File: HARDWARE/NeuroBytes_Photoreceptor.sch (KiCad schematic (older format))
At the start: 21 parts, among them P1 CONN_01X04, P2 CONN_01X04, P3 CONN_01X07, SW1 SW_PUSH, SW2 SW_PUSH, U1 APDS9007, U2 STM32L011Gx, U3 LD3985M33R

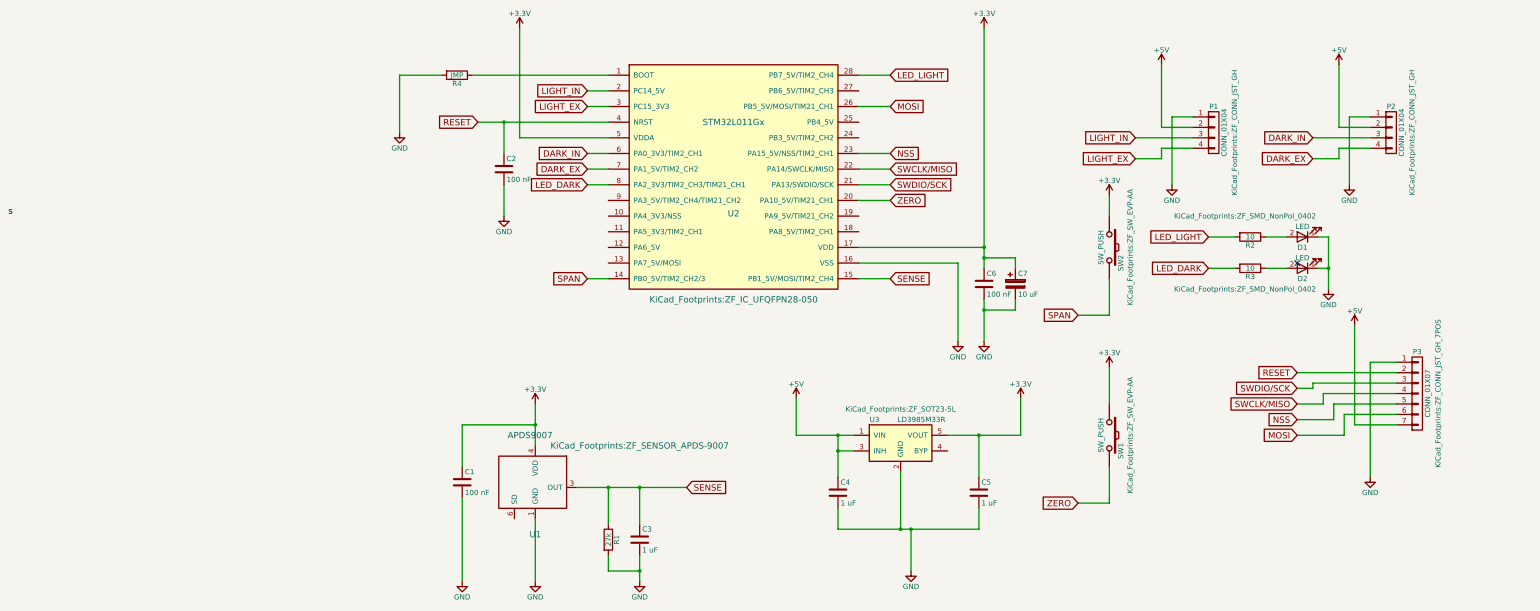
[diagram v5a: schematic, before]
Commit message: Another switch footprint update
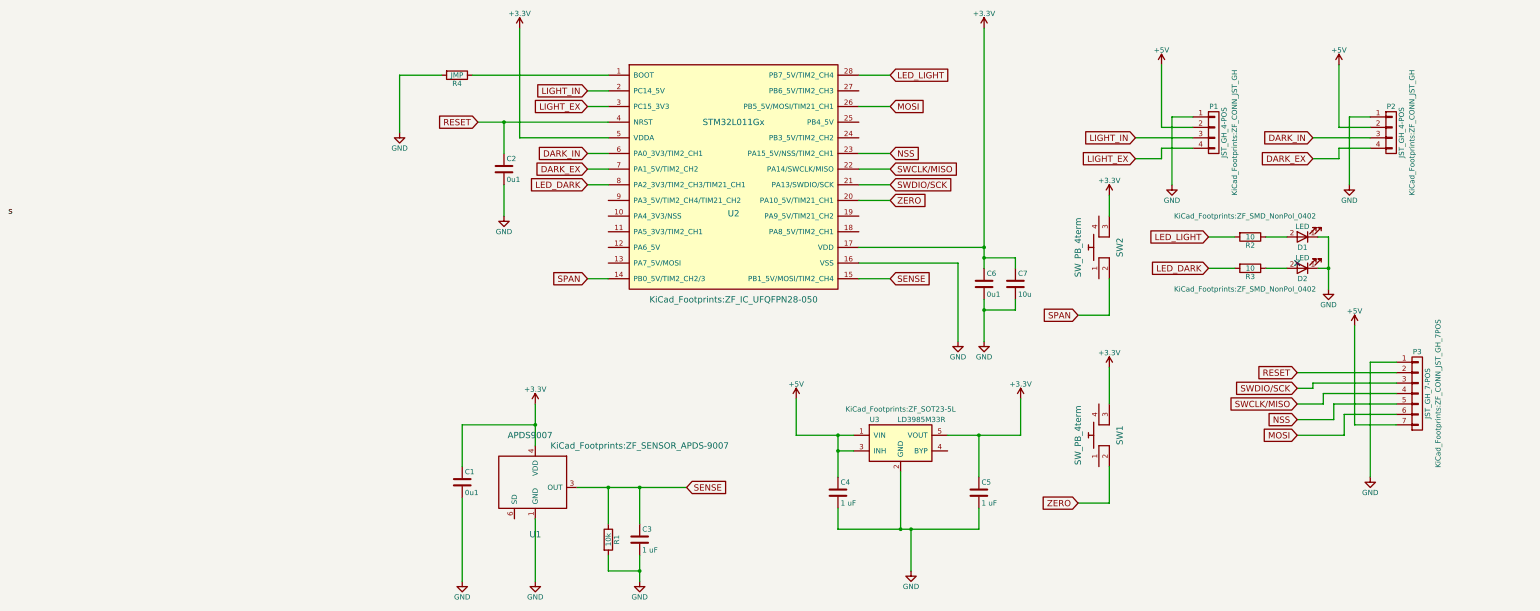
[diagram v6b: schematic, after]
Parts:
- removed C7: 10 uF, KiCad_Footprints:ZF_SMD_pol_1206, symbol CP
- removed SW1, SW2: SW_PUSH, KiCad_Footprints:ZF_SW_EVP-AA, symbol SW_PUSH
- added C7: 10u, KiCad_Footprints:ZF_SMD_nonpol_1206, symbol C
- added SW1, SW2: SW_PB_4term, KiCad_Footprints:ZF_SW_PTS810, symbol SW_PB_4term
- C1, C2, C6: value 100 nF -> 0u1; Mfr Part # (none) -> MF-CAP-0402-0.1uF; Package (none) -> C0402
- C3, C4, C5: Mfr Part # (none) -> MF-CAP-0603-1uF; Package (none) -> C0603
- D1, D2: Mfr Part # (none) -> SCMP13WBC8W1; Package (none) -> 2SMD
- P1, P2: value CONN_01X04 -> JST_GH_4-POS; Mfr Part # (none) -> SM04B-GHS-GD-TB(LF)(SN); Package (none) -> JST_GH_4-POS
- P3: value CONN_01X07 -> JST_GH_7-POS; Mfr Part # (none) -> SM07B-GHS-TB(LF)(SN); Package (none) -> JST_GH_7-POS
- R1: value 27k -> 10k; Mfr Part # (none) -> MF-RES-0402-10K; Package (none) -> R0402
- R2, R3: Mfr Part # (none) -> MF-RES-0402-10; Package (none) -> R0402
- R4: Mfr Part # (none) -> MF-RES-0402-0; Package (none) -> R0402
- U1: Mfr Part # (none) -> APDS-9007-020; Package (none) -> 6SMD
- U2: Mfr Part # (none) -> STM32L011G4U6; Package (none) -> UFQFPN28
- U3: Mfr Part # (none) -> MF-REG-SOT235-3.3V-300mA; Package (none) -> SOT23-5L
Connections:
- net +3V3: now also C7.1, SW1.3, SW2.3
- net GND: now also C7.2
- net SPAN: now also SW2.2
- net ZERO: now also SW1.2

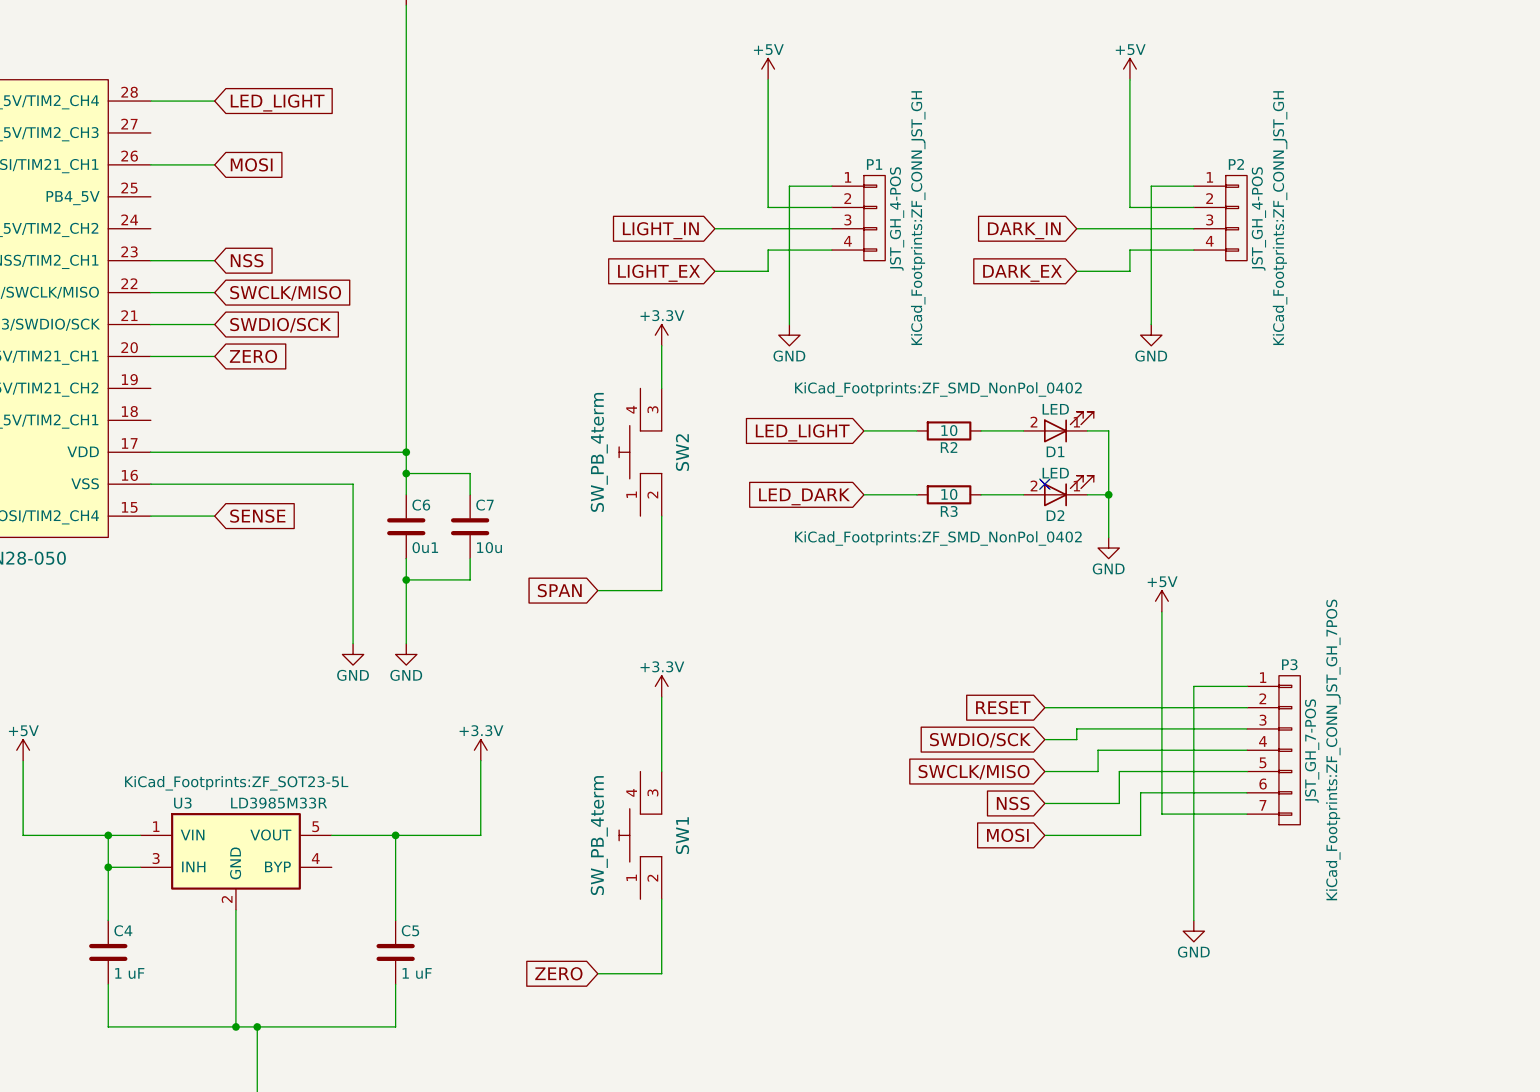
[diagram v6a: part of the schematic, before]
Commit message: Changed to 5-pin JST GH connector for programming and power. Added POWER label. Minor routing changes.
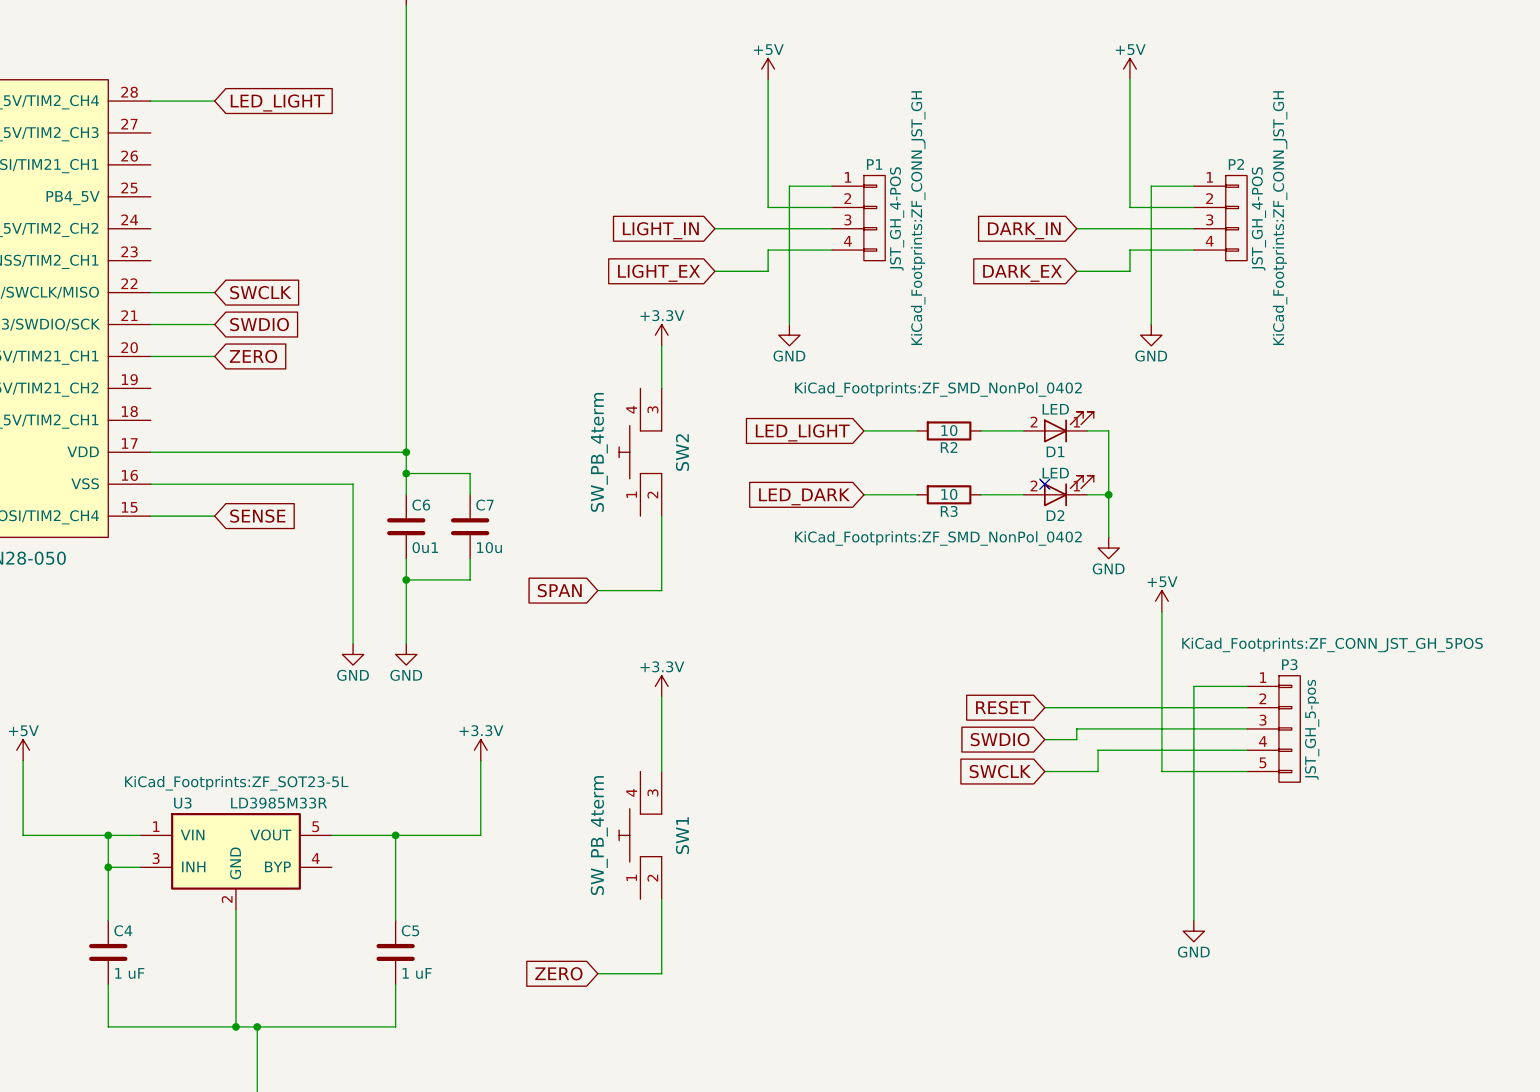
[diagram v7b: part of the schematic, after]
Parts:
- removed P3: JST_GH_7-POS, KiCad_Footprints:ZF_CONN_JST_GH_7POS, symbol CONN_01X07
- added P3: JST_GH_5-pos, KiCad_Footprints:ZF_CONN_JST_GH_5POS, symbol CONN_01X05
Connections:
- net +5V: now also P3.5 (P5)
- net GND: now also P3.1 (P1)
- net RESET: now also P3.2 (P2)
- net MOSI: no longer names the net of U2.26 (PB5_5V/MOSI/TIM21_CH1)
- net NSS: no longer names the net of U2.23 (PA15_5V/NSS/TIM2_CH1)
- net SWCLK/MISO renamed SWCLK
- net SWCLK: now also P3.4 (P4)
- net SWDIO/SCK renamed SWDIO
- net SWDIO: now also P3.3 (P3)
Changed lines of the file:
@@
 $EndComp
 $Comp
-L +5V #PWR01
+L +5V #PWR8
 U 1 1 58B9AB7F
 P 4700 4850
-F 0 "#PWR01" H 4700 4700 50  0001 C CNN
+F 0 "#PWR8" H 4700 4700 50  0001 C CNN
 F 1 "+5V" H 4700 4990 50  0000 C CNN
 F 2 "" H 4700 4850 50  0000 C CNN
@@
 $EndComp
 $Comp
-L +3.3V #PWR02
+L +3.3V #PWR13
 U 1 1 58B9B0DC
 P 6850 4850
-F 0 "#PWR02" H 6850 4700 50  0001 C CNN
+F 0 "#PWR13" H 6850 4700 50  0001 C CNN
 F 1 "+3.3V" H 6850 4990 50  0000 C CNN
 F 2 "" H 6850 4850 50  0000 C CNN
@@
 $EndComp
 $Comp
-L GND #PWR03
+L GND #PWR9
 U 1 1 58B9B110
 P 5800 6500
-F 0 "#PWR03" H 5800 6250 50  0001 C CNN
+F 0 "#PWR9" H 5800 6250 50  0001 C CNN
 F 1 "GND" H 5800 6350 50  0000 C CNN
 F 2 "" H 5800 6500 50  0000 C CNN
@@
 $EndComp
 $Comp
-L +3.3V #PWR04
+L +3.3V #PWR4
 U 1 1 58B9B1C8
 P 2050 1300
-F 0 "#PWR04" H 2050 1150 50  0001 C CNN
+F 0 "#PWR4" H 2050 1150 50  0001 C CNN
 F 1 "+3.3V" H 2050 1440 50  0000 C CNN
 F 2 "" H 2050 1300 50  0000 C CNN
@@
 $EndComp
 $Comp
-L +3.3V #PWR05
+L +3.3V #PWR11
 U 1 1 58B9B218
 P 6500 1300
-F 0 "#PWR05" H 6500 1150 50  0001 C CNN
+F 0 "#PWR11" H 6500 1150 50  0001 C CNN
 F 1 "+3.3V" H 6500 1440 50  0000 C CNN
 F 2 "" H 6500 1300 50  0000 C CNN
@@
 $EndComp
 $Comp
-L GND #PWR06
+L GND #PWR10
 U 1 1 58B9B234
 P 6250 4300
-F 0 "#PWR06" H 6250 4050 50  0001 C CNN
+F 0 "#PWR10" H 6250 4050 50  0001 C CNN
 F 1 "GND" H 6250 4150 50  0000 C CNN
 F 2 "" H 6250 4300 50  0000 C CNN
@@
 $EndComp
 $Comp
-L GND #PWR07
+L GND #PWR3
 U 1 1 58B9B2B4
 P 1900 3100
-F 0 "#PWR07" H 1900 2850 50  0001 C CNN
+F 0 "#PWR3" H 1900 2850 50  0001 C CNN
 F 1 "GND" H 1900 2950 50  0000 C CNN
 F 2 "" H 1900 3100 50  0000 C CNN
@@
 Wire Wire Line
 	5300 3550 6250 3550
-$Comp
-L CONN_01X07 P3
-U 1 1 58B9B3B2
-P 10650 4800
-F 0 "P3" H 10650 5200 50  0000 C CNN
-F 1 "JST_GH_7-POS" V 10750 4800 50  0000 C CNN
-F 2 "KiCad_Footprints:ZF_CONN_JST_GH_7POS" V 10850 4800 50  0000 C CNN
-F 3 "" H 10650 4800 50  0000 C CNN
-F 4 "SM07B-GHS-TB(LF)(SN)" H 10650 4800 60  0001 C CNN "Mfr Part #"
-F 5 "JST_GH_7-POS" H 10650 4800 60  0001 C CNN "Package"
-F 6 "No" H 10650 4800 60  0001 C CNN "Subs Allowed"
-F 7 "Yes" H 10650 4800 60  0001 C CNN "RoHS"
-	1    10650 4800
-	1    0    0    -1
-$EndComp
 Text GLabel 5600 2650 2    60   Input ~ 0
-SWCLK/MISO
+SWCLK
 Wire Wire Line
 	5600 2650 5300 2650
 Wire Wire Line
 	6500 1300 6500 3600
-Text GLabel 5600 2500 2    60   Input ~ 0
-NSS
-Wire Wire Line
-	5600 2500 5300 2500
-Text GLabel 5600 2050 2    60   Input ~ 0
-MOSI
-Wire Wire Line
-	5600 2050 5300 2050
 Text GLabel 1650 2200 0    60   Input ~ 0
 RESET
@@
 	1650 2200 2900 2200
 Text GLabel 5600 2800 2    60   Input ~ 0
-SWDIO/SCK
+SWDIO
 Wire Wire Line
 	5600 2800 5300 2800
 $Comp
-L +5V #PWR08
+L +5V #PWR21
 U 1 1 58B9B77D
 P 10050 4150
-F 0 "#PWR08" H 10050 4000 50  0001 C CNN
+F 0 "#PWR21" H 10050 4000 50  0001 C CNN
 F 1 "+5V" H 10050 4290 50  0000 C CNN
 F 2 "" H 10050 4150 50  0000 C CNN
@@
 $EndComp
 $Comp
-L GND #PWR09
+L GND #PWR22
 U 1 1 58B9B796
 P 10200 5600
-F 0 "#PWR09" H 10200 5350 50  0001 C CNN
+F 0 "#PWR22" H 10200 5350 50  0001 C CNN
 F 1 "GND" H 10200 5450 50  0000 C CNN
 F 2 "" H 10200 5600 50  0000 C CNN
@@
 	1    0    0    -1
 $EndComp
-Text GLabel 9500 5200 0    60   Input ~ 0
-MOSI
-Text GLabel 9500 5050 0    60   Input ~ 0
-NSS
 Text GLabel 9500 4900 0    60   Input ~ 0
-SWCLK/MISO
+SWCLK
 Text GLabel 9500 4750 0    60   Input ~ 0
-SWDIO/SCK
+SWDIO
 Text GLabel 9500 4600 0    60   Input ~ 0
 RESET
@@
 Wire Wire Line
 	9750 4900 9500 4900
-Wire Wire Line
-	10450 4900 9850 4900
-Wire Wire Line
-	9850 4900 9850 5050
-Wire Wire Line
-	9850 5050 9500 5050
-Wire Wire Line
-	10450 5000 9950 5000
-Wire Wire Line
-	9950 5000 9950 5200
-Wire Wire Line
-	9950 5200 9500 5200
-Wire Wire Line
-	10450 5100 10050 5100
-Wire Wire Line
-	10050 5100 10050 4150
 Connection ~ 6500 3400
 $Comp
-L GND #PWR010
+L GND #PWR12
 U 1 1 58B9C6F5
 P 6500 4300
-F 0 "#PWR010" H 6500 4050 50  0001 C CNN
+F 0 "#PWR12" H 6500 4050 50  0001 C CNN
 F 1 "GND" H 6500 4150 50  0000 C CNN
 F 2 "" H 6500 4300 50  0000 C CNN
@@
 $EndComp
 $Comp
-L +5V #PWR011
+L +5V #PWR19
 U 1 1 58B9CBAC
 P 9900 1650
-F 0 "#PWR011" H 9900 1500 50  0001 C CNN
+F 0 "#PWR19" H 9900 1500 50  0001 C CNN
 F 1 "+5V" H 9900 1790 50  0000 C CNN
 F 2 "" H 9900 1650 50  0000 C CNN
@@
 	9900 2250 10200 2250
 $Comp
-L GND #PWR012
+L GND #PWR20
 U 1 1 58B9CC0C
 P 10000 2800
-F 0 "#PWR012" H 10000 2550 50  0001 C CNN
+F 0 "#PWR20" H 10000 2550 50  0001 C CNN
 F 1 "GND" H 10000 2650 50  0000 C CNN
 F 2 "" H 10000 2800 50  0000 C CNN
@@
 $EndComp
 $Comp
-L +5V #PWR013
+L +5V #PWR16
 U 1 1 58B9CEA4
 P 8200 1650
-F 0 "#PWR013" H 8200 1500 50  0001 C CNN
+F 0 "#PWR16" H 8200 1500 50  0001 C CNN
 F 1 "+5V" H 8200 1790 50  0000 C CNN
 F 2 "" H 8200 1650 50  0000 C CNN
@@
 	8200 2250 8500 2250
 $Comp
-L GND #PWR014
+L GND #PWR17
 U 1 1 58B9CEAC
 P 8300 2800
-F 0 "#PWR014" H 8300 2550 50  0001 C CNN
+F 0 "#PWR17" H 8300 2550 50  0001 C CNN
 F 1 "GND" H 8300 2650 50  0000 C CNN
 F 2 "" H 8300 2800 50  0000 C CNN
@@
 $EndComp
 $Comp
-L GND #PWR015
+L GND #PWR18
 U 1 1 58B9D2D7
 P 9800 3800
-F 0 "#PWR015" H 9800 3550 50  0001 C CNN
+F 0 "#PWR18" H 9800 3550 50  0001 C CNN
 F 1 "GND" H 9800 3650 50  0000 C CNN
 F 2 "" H 9800 3800 50  0000 C CNN
@@
 ZERO
 $Comp
-L +3.3V #PWR016
+L +3.3V #PWR15
 U 1 1 58B9D7AB
 P 7700 4550
-F 0 "#PWR016" H 7700 4400 50  0001 C CNN
+F 0 "#PWR15" H 7700 4400 50  0001 C CNN
 F 1 "+3.3V" H 7700 4690 50  0000 C CNN
 F 2 "" H 7700 4550 50  0000 C CNN
@@
 SPAN
 $Comp
-L +3.3V #PWR017
+L +3.3V #PWR14
 U 1 1 58B9D91D
 P 7700 2900
-F 0 "#PWR017" H 7700 2750 50  0001 C CNN
+F 0 "#PWR14" H 7700 2750 50  0001 C CNN
 F 1 "+3.3V" H 7700 3040 50  0000 C CNN
 F 2 "" H 7700 2900 50  0000 C CNN
@@
 $EndComp
 $Comp
-L +3.3V #PWR018
+L +3.3V #PWR5
 U 1 1 58B9DDBA
 P 2200 4900
-F 0 "#PWR018" H 2200 4750 50  0001 C CNN
+F 0 "#PWR5" H 2200 4750 50  0001 C CNN
 F 1 "+3.3V" H 2200 5040 50  0000 C CNN
 F 2 "" H 2200 4900 50  0000 C CNN
@@
 	2200 4900 2200 5300
 $Comp
-L GND #PWR019
+L GND #PWR6
 U 1 1 58B9DE4B
 P 2200 6600
-F 0 "#PWR019" H 2200 6350 50  0001 C CNN
+F 0 "#PWR6" H 2200 6350 50  0001 C CNN
 F 1 "GND" H 2200 6450 50  0000 C CNN
 F 2 "" H 2200 6600 50  0000 C CNN
@@
 $EndComp
 $Comp
-L GND #PWR020
+L GND #PWR7
 U 1 1 58B9DF7E
 P 3200 6600
-F 0 "#PWR020" H 3200 6350 50  0001 C CNN
+F 0 "#PWR7" H 3200 6350 50  0001 C CNN
 F 1 "GND" H 3200 6450 50  0000 C CNN
 F 2 "" H 3200 6600 50  0000 C CNN
@@
 Connection ~ 2200 5100
 $Comp
-L GND #PWR021
+L GND #PWR2
 U 1 1 58B9E313
 P 1500 6600
-F 0 "#PWR021" H 1500 6350 50  0001 C CNN
+F 0 "#PWR2" H 1500 6350 50  0001 C CNN
 F 1 "GND" H 1500 6450 50  0000 C CNN
 F 2 "" H 1500 6600 50  0000 C CNN
@@
 $EndComp
 $Comp
-L GND #PWR022
+L GND #PWR1
 U 1 1 590B4A9C
 P 900 2300
-F 0 "#PWR022" H 900 2050 50  0001 C CNN
+F 0 "#PWR1" H 900 2050 50  0001 C CNN
 F 1 "GND" H 900 2150 50  0000 C CNN
 F 2 "" H 900 2300 50  0000 C CNN
@@
 	0    -1   -1   0
 $EndComp
+$Comp
+L CONN_01X05 P3
+U 1 1 598DF7CF
+P 10650 4700
+F 0 "P3" H 10650 5000 50  0000 C CNN
+F 1 "JST_GH_5-pos" V 10750 4700 50  0000 C CNN
+F 2 "KiCad_Footprints:ZF_CONN_JST_GH_5POS" H 10850 5100 50  0000 C CNN
+F 3 "" H 10650 4700 50  0000 C CNN
+F 4 "No" H 10650 4700 60  0001 C CNN "Subs Allowed"
+F 5 "Yes" H 10650 4700 60  0001 C CNN "RoHS"
+	1    10650 4700
+	1    0    0    -1
+$EndComp
+Wire Wire Line
+	10450 4900 10050 4900
+Wire Wire Line
+	10050 4900 10050 4150
 $EndSCHEMATC

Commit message: updated component descriptions. reloaded netlist. minor PCB updates. fresh *.csv export.
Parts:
- C1, C2, C6: Link (none) -> https://www.digikey.com/product-detail/en/taiyo-yuden/LMK10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; Mfr (none) -> Taiyo Yuden; Mfr Part # MF-CAP-0402-0.1uF -> LMK105BJ104KV-F
- C3, C4, C5: value 1 uF -> 1u; Link (none) -> https://www.digikey.com/product-detail/en/taiyo-yuden/LMK10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; Mfr (none) -> Taiyo Yuden; Mfr Part # MF-CAP-0603-1uF -> LMK107B7105KA-T
- C7: Link (none) -> https://www.digikey.com/product-detail/en/taiyo-yuden/EMK31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; Mfr (none) -> Taiyo Yuden; Mfr Part # MF-CAP-1206-10uF -> EMK316B7106KL-TD; Subs Allowed No -> Yes
- D1, D2: Link (none) -> https://www.digikey.com/product-detail/en/rohm-semiconducto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; Mfr (none) -> Rohm Semiconductor
- P1, P2: Link (none) -> https://www.digikey.com/product-detail/en/jst-sales-america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; Mfr (none) -> JST; Mfr Part # SM04B-GHS-GD-TB(LF)(SN) -> SM04B-GHS-TB(LF)(SN); Package JST_GH_4-POS -> SMT
- P3: Link (none) -> https://www.digikey.com/product-detail/en/jst-sales-america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; Mfr (none) -> JST; Mfr Part # (none) -> SM05B-GHS-TB(LF)(SN); Package (none) -> SMT
- R1: Link (none) -> https://www.digikey.com/product-detail/en/yageo/RC0402FR-07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; Mfr (none) -> Yageo; Mfr Part # MF-RES-0402-10K -> RC0402FR-0710KL
- R2, R3: Link (none) -> https://www.digikey.com/product-detail/en/yageo/RC0402FR-07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; Mfr (none) -> Yageo; Mfr Part # MF-RES-0402-10 -> RC0402FR-0710RL
- R4: Link (none) -> https://www.digikey.com/product-detail/en/yageo/RC0402JR-07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; Mfr (none) -> Yageo; Mfr Part # MF-RES-0402-0 -> RC0402JR-070RL
- SW1, SW2: Link (none) -> https://www.digikey.com/product-detail/en/c-k/PTS810-SJM-25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; Mfr (none) -> C&K; Mfr Part # MF-SW-TACT-4.2MM -> PTS810 SJM 250 SMTR LFS
- U1: Link (none) -> https://www.digikey.com/product-detail/en/broadcom-limited/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; Mfr (none) -> Broadcom
- U2: Link (none) -> http://www.mouser.com/ProductDetail/STMicroelectronics/STM3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; Mfr (none) -> ST Microelectronics
- U3: value LD3985M33R -> 3v3 LDO; Link (none) -> https://www.digikey.com/product-detail/en/on-semiconductor/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; Mfr (none) -> ON Semiconductor; Mfr Part # MF-REG-SOT235-3.3V-300mA -> NCP114BSN330T1G; Subs Allowed No -> Yes
